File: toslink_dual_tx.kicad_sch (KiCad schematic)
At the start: 20 parts, among them J1 Conn_01x04_Pin, J2 Conn_01x01_Pin, J3 Conn_01x06_Pin, J4 Conn_01x06_Pin, U1 L7805, U2 74HC86, U3 74HC00

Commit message: changed from DIL to SO-14 ICs
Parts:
- U2, U3: footprint Package_DIP:DIP-14_W7.62mm -> Package_SO:SO-14_5.3x10.2mm_P1.27mm
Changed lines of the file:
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@@
 			)
 		)
-		(property "Footprint" "Package_DIP:DIP-14_W7.62mm"
+		(property "Footprint" "Package_SO:SO-14_5.3x10.2mm_P1.27mm"
 			(at 124.46 29.21 0)
 			(effects
@@
 			)
 		)
-		(property "Footprint" "Package_DIP:DIP-14_W7.62mm"
+		(property "Footprint" "Package_SO:SO-14_5.3x10.2mm_P1.27mm"
 			(at 105.41 102.87 0)
 			(effects
@@
 			)
 		)
-		(property "Footprint" "Package_DIP:DIP-14_W7.62mm"
+		(property "Footprint" "Package_SO:SO-14_5.3x10.2mm_P1.27mm"
 			(at 74.93 62.23 0)
 			(effects
@@
 			)
 		)
-		(property "Footprint" "Package_DIP:DIP-14_W7.62mm"
+		(property "Footprint" "Package_SO:SO-14_5.3x10.2mm_P1.27mm"
 			(at 59.69 62.23 0)
 			(effects
@@
 			)
 		)
-		(property "Footprint" "Package_DIP:DIP-14_W7.62mm"
+		(property "Footprint" "Package_SO:SO-14_5.3x10.2mm_P1.27mm"
 			(at 59.69 111.76 0)
 			(effects
@@
 			)
 		)
-		(property "Footprint" "Package_DIP:DIP-14_W7.62mm"
+		(property "Footprint" "Package_SO:SO-14_5.3x10.2mm_P1.27mm"
 			(at 83.82 100.33 0)
 			(effects
@@
 			)
 		)
-		(property "Footprint" "Package_DIP:DIP-14_W7.62mm"
+		(property "Footprint" "Package_SO:SO-14_5.3x10.2mm_P1.27mm"
 			(at 91.44 62.23 0)
 			(effects
@@
 			)
 		)
-		(property "Footprint" "Package_DIP:DIP-14_W7.62mm"
+		(property "Footprint" "Package_SO:SO-14_5.3x10.2mm_P1.27mm"
 			(at 147.32 29.21 0)
 			(effects
@@
 			)
 		)
-		(property "Footprint" "Package_DIP:DIP-14_W7.62mm"
+		(property "Footprint" "Package_SO:SO-14_5.3x10.2mm_P1.27mm"
 			(at 58.42 92.71 0)
 			(effects
@@
 			)
 		)
-		(property "Footprint" "Package_DIP:DIP-14_W7.62mm"
+		(property "Footprint" "Package_SO:SO-14_5.3x10.2mm_P1.27mm"
 			(at 118.11 127 0)
 			(effects

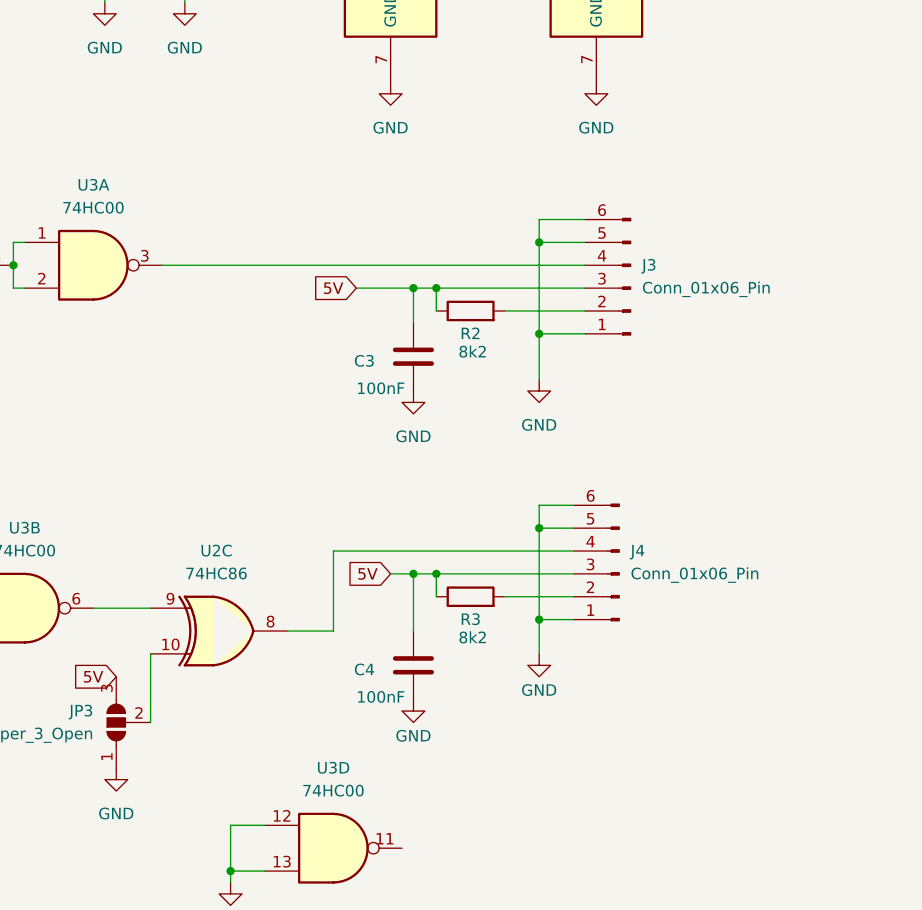
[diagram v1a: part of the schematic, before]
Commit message: added TOTX173 symbols and footprints
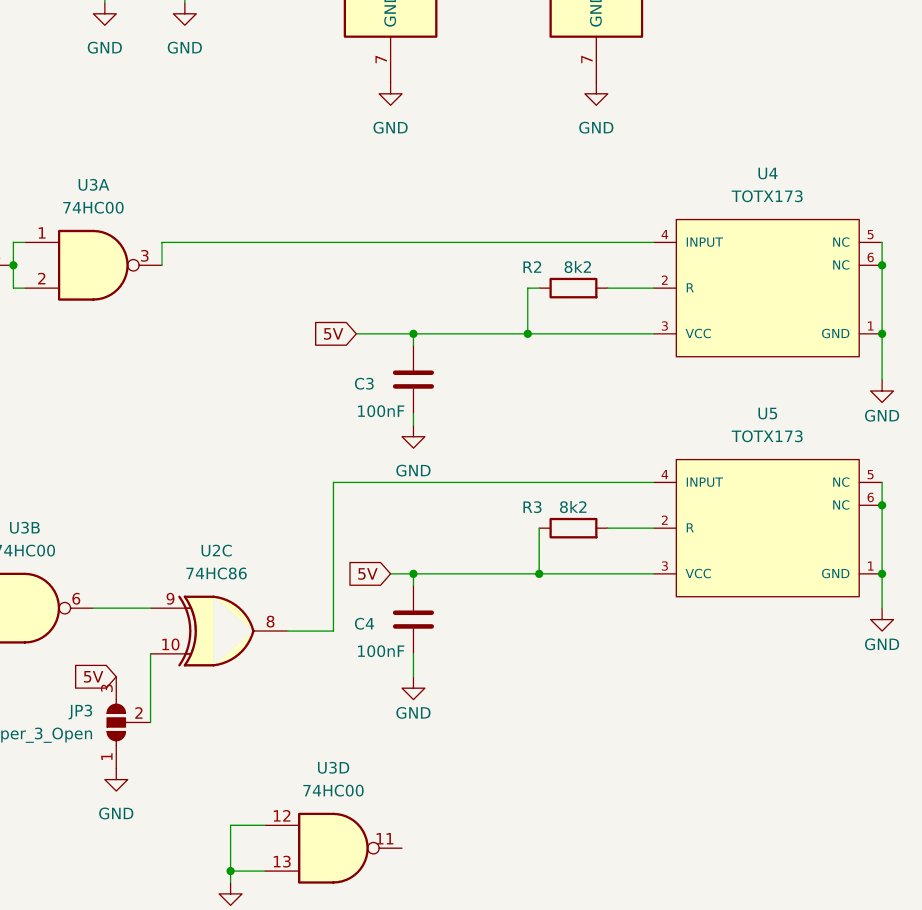
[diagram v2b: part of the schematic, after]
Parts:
- removed J3, J4: Conn_01x06_Pin, Connector_PinHeader_2.54mm:PinHeader_1x06_P2.54mm_Vertical, symbol Connector:Conn_01x06_Pin
- added U4, U5: TOTX173, OptoDevice:Toshiba_TOTX170_TOTX173_TOTX193_TOTX194, symbol TOTX173:TOTX173
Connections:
- net 5V: now also U4.3 (VCC), U5.3 (VCC)
- net GND: now also U4.1 (GND), U4.5 (NC), U4.6 (NC), U5.1 (GND), U5.5 (NC), U5.6 (NC)
- net at R3.2: now also U5.2 (R)
- net at U2.8: now also U5.4 (INPUT)
- net at R2.2: now also U4.2 (R)
- net at U3.3: now also U4.4 (INPUT)
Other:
- moved on the sheet: C3, C4, R2, R3

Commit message: added mounting holes, shrink size, added jumpers to bridge the logic gates
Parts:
- added H1, H2, H3, H4: MountingHole, MountingHole:MountingHole_3.2mm_M3, symbol Mechanical:MountingHole
- added JP4, JP5: SolderJumper_2_Open, Jumper:SolderJumper-2_P1.3mm_Open_Pad1.0x1.5mm, symbol Jumper:SolderJumper_2_Open
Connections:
- net CLOCK: now also JP5.1 (A)
- net DATA: now also JP4.1 (A)
- net at U2.8, U5.4 (INPUT): now also JP5.2 (B)
- net at U3.3, U4.4 (INPUT): now also JP4.2 (B)
